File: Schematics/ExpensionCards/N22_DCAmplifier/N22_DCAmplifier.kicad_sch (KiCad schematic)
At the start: 81 parts

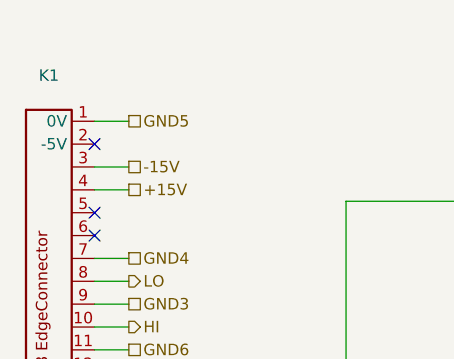
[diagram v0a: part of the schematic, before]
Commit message: Reworked N20/N21
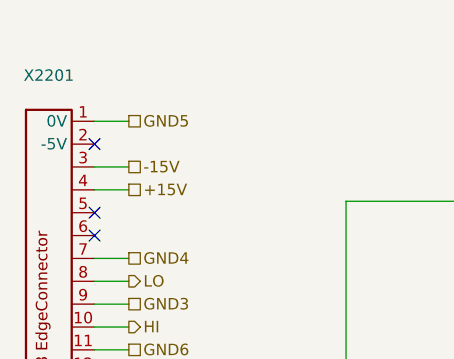
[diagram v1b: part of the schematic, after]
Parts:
- JP2201: renamed from JP2; footprint TestPoint:TestPoint_Bridge_Pitch2.54mm_Drill1.0mm -> TestPoint:TestPoint_Bridge_Pitch5.08mm_Drill0.7mm
- JP2202: renamed from JP1; footprint TestPoint:TestPoint_Bridge_Pitch2.54mm_Drill1.0mm -> TestPoint:TestPoint_Bridge_Pitch5.08mm_Drill0.7mm
- R2209, R2214, R2216, R2217, R2232: footprint PM2528:Potentiometer horizontal ceramic -> PM2528:Trimmer vertical
- renumbered K1 to X2201
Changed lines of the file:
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@@
 		(on_board yes)
 		(dnp no)
-		(property "Reference" "JP2"
+		(property "Reference" "JP2201"
 			(at 90.17 199.39 0)
 			(effects
@@
 			)
 		)
-		(property "Footprint" "TestPoint:TestPoint_Bridge_Pitch2.54mm_Drill1.0mm"
+		(property "Footprint" "TestPoint:TestPoint_Bridge_Pitch5.08mm_Drill0.7mm"
 			(at 90.17 205.74 0)
 			(effects
@@
 			(project "N22_DCAmplifier"
 				(path "/2ba4ca6b-4aec-411c-9da4-218d92fedde9"
-					(reference "JP2")
+					(reference "JP2201")
 					(unit 1)
 				)
@@
 			)
 		)
-		(property "Footprint" "PM2528:Potentiometer horizontal ceramic"
+		(property "Footprint" "PM2528:Trimmer vertical"
 			(at 156.21 193.04 0)
 			(effects
@@
 		(on_board yes)
 		(dnp no)
-		(property "Reference" "JP1"
+		(property "Reference" "JP2202"
 			(at 77.47 199.39 0)
 			(effects
@@
 			)
 		)
-		(property "Footprint" "TestPoint:TestPoint_Bridge_Pitch2.54mm_Drill1.0mm"
+		(property "Footprint" "TestPoint:TestPoint_Bridge_Pitch5.08mm_Drill0.7mm"
 			(at 77.47 205.74 0)
 			(effects
@@
 			(project ""
 				(path "/2ba4ca6b-4aec-411c-9da4-218d92fedde9"
-					(reference "JP1")
+					(reference "JP2202")
 					(unit 1)
 				)
@@
 			)
 		)
-		(property "Footprint" "PM2528:Potentiometer horizontal ceramic"
+		(property "Footprint" "PM2528:Trimmer vertical"
 			(at 110.49 209.55 0)
 			(effects
@@
 			)
 		)
-		(property "Footprint" "PM2528:Potentiometer horizontal ceramic"
+		(property "Footprint" "PM2528:Trimmer vertical"
 			(at 95.25 120.65 0)
 			(effects
@@
 			)
 		)
-		(property "Footprint" "PM2528:Potentiometer horizontal ceramic"
+		(property "Footprint" "PM2528:Trimmer vertical"
 			(at 172.72 88.9 0)
 			(effects
@@
 			)
 		)
-		(property "Footprint" "PM2528:Potentiometer horizontal ceramic"
+		(property "Footprint" "PM2528:Trimmer vertical"
 			(at 76.2 261.62 0)
 			(effects
@@
 		(dnp no)
 		(fields_autoplaced yes)
-		(property "Reference" "K1"
+		(property "Reference" "X2201"
 			(at 20.32 20.32 0)
 			(effects
@@
 					(size 1.27 1.27)
 				)
+				(hide yes)
 			)
 		)
@@
 			(project ""
 				(path "/2ba4ca6b-4aec-411c-9da4-218d92fedde9"
-					(reference "K1")
+					(reference "X2201")
 					(unit 1)
 				)

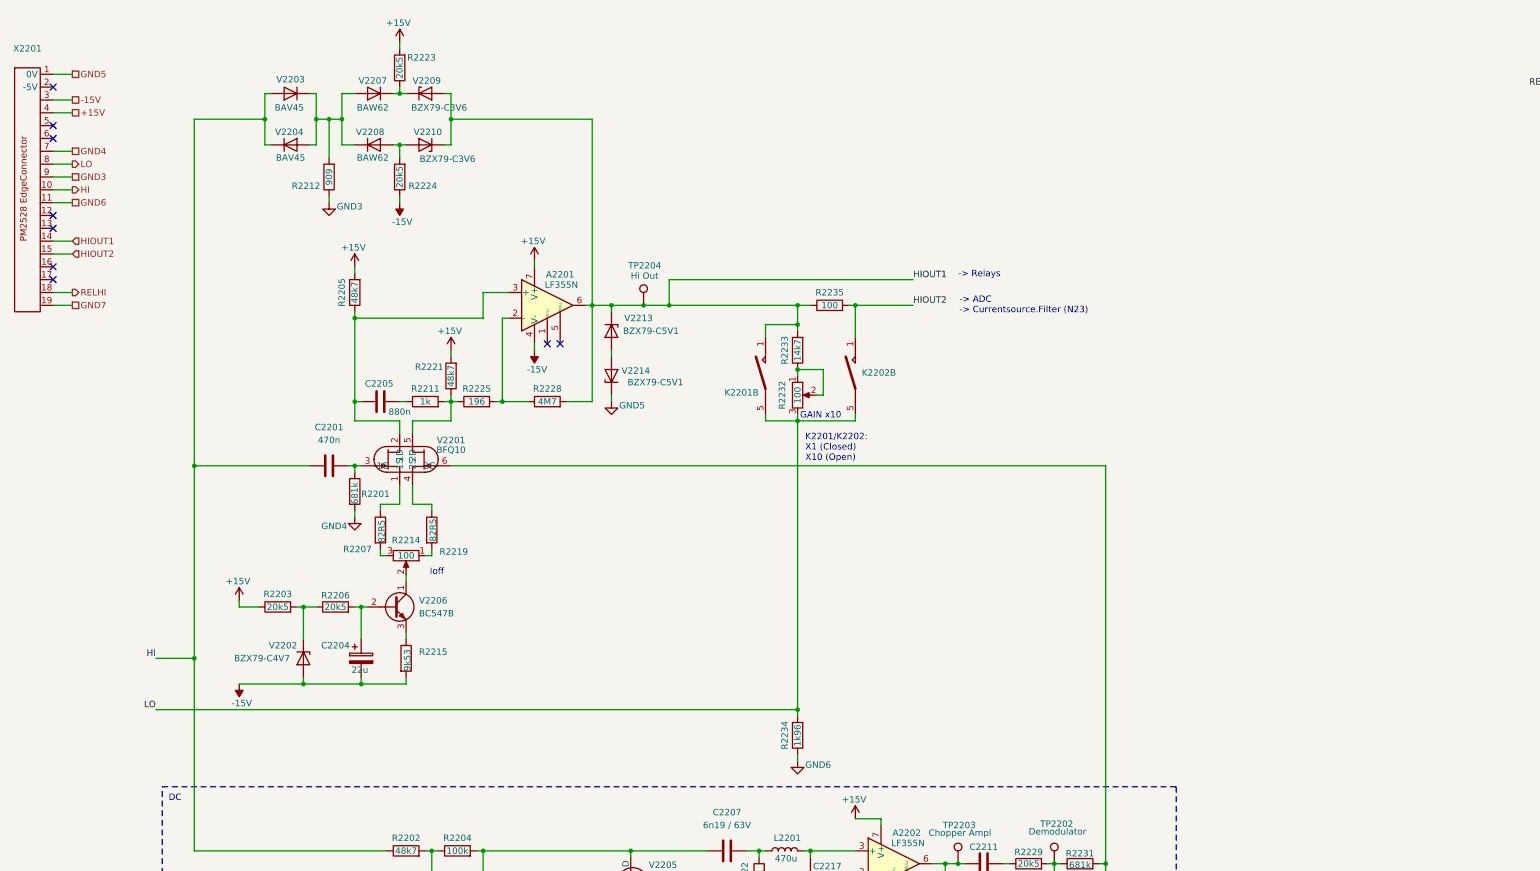
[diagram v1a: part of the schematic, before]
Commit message: Small modifications, more disassembly
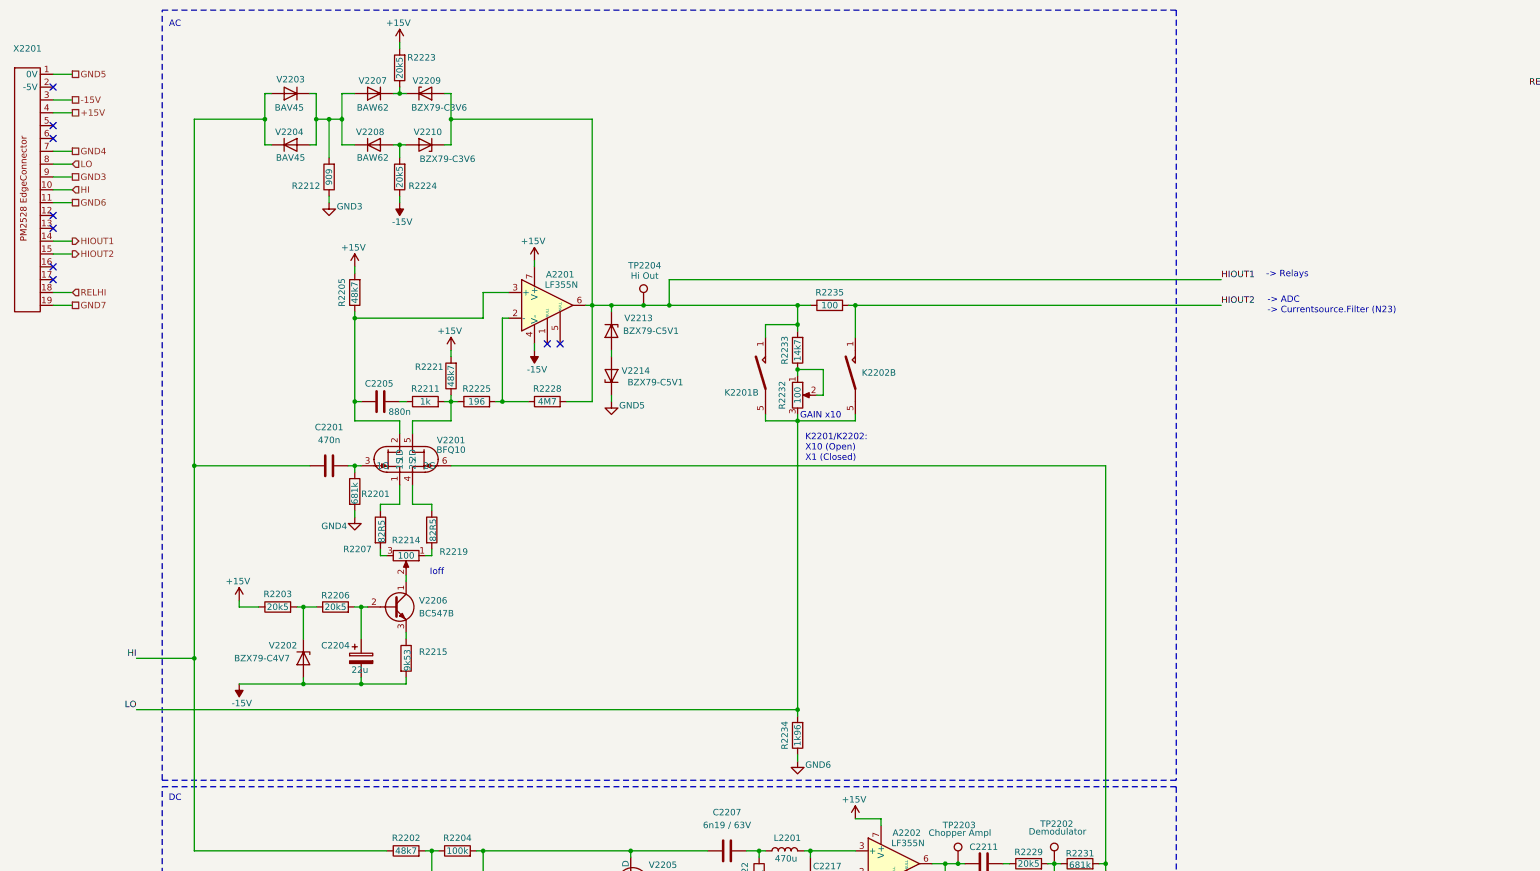
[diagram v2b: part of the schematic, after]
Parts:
- V2203, V2204: footprint Diode_THT:D_DO-35_SOD27_P5.08mm_Vertical_AnodeUp -> Diode_THT:D_DO-35_SOD27_P7.62mm_Horizontal
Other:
- note added: "AC"
- note added: "K2201/K2202: X10 (Open) X1 (Closed)"
- note removed: "K2201/K2202: X1 (Closed) X10 (Open)"
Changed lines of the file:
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@@
 	)
 	(rectangle
+		(start 46.99 12.7)
+		(end 247.65 165.1)
+		(stroke
+			(width 0)
+			(type dash_dot_dot)
+		)
+		(fill
+			(type none)
+		)
+	)
+	(rectangle
 		(start 46.99 218.44)
 		(end 144.78 281.94)
@@
 	(text "-> Relays"
 		(exclude_from_sim no)
-		(at 204.47 65.024 0)
+		(at 265.43 65.024 0)
 		(effects
 			(font
@@
 	(text "-> ADC\n-> Currentsource.Filter (N23)\n"
 		(exclude_from_sim no)
-		(at 204.724 71.12 0)
+		(at 265.684 71.12 0)
 		(effects
 			(font
@@
 		)
 	)
-	(text "K2201/K2202:\nX1 (Closed)\nX10 (Open)"
+	(text "K2201/K2202:\nX10 (Open)\nX1 (Closed)\n"
 		(exclude_from_sim no)
 		(at 174.244 99.314 0)
@@
 		)
 	)
+	(text "AC"
+		(exclude_from_sim no)
+		(at 49.53 15.494 0)
+		(effects
+			(font
+				(size 1.27 1.27)
+			)
+		)
+	)
 	(text "Power"
 		(exclude_from_sim no)
@@
 	(wire
 		(pts
-			(xy 195.58 66.04) (xy 147.32 66.04)
+			(xy 256.54 66.04) (xy 147.32 66.04)
 		)
 		(stroke
@@
 	(wire
 		(pts
-			(xy 184.15 71.12) (xy 195.58 71.12)
+			(xy 184.15 71.12) (xy 256.54 71.12)
 		)
 		(stroke
@@
 	(wire
 		(pts
-			(xy 45.72 140.97) (xy 53.34 140.97)
+			(xy 41.91 140.97) (xy 53.34 140.97)
 		)
 		(stroke
@@
 	(wire
 		(pts
-			(xy 45.72 151.13) (xy 172.72 151.13)
+			(xy 41.91 151.13) (xy 172.72 151.13)
 		)
 		(stroke
@@
 	)
 	(label "HI"
-		(at 45.72 140.97 180)
+		(at 41.91 140.97 180)
 		(effects
 			(font
@@
 	)
 	(label "HIOUT1"
-		(at 195.58 66.04 0)
+		(at 256.54 66.04 0)
 		(effects
 			(font
@@
 	)
 	(label "LO"
-		(at 45.72 151.13 180)
+		(at 41.91 151.13 180)
 		(effects
 			(font
@@
 	)
 	(label "HIOUT2"
-		(at 195.58 71.12 0)
+		(at 256.54 71.12 0)
 		(effects
 			(font
@@
 	)
 	(hierarchical_label "HIOUT2"
-		(shape input)
+		(shape output)
 		(at 29.21 60.96 0)
 		(effects
@@
 	)
 	(hierarchical_label "HI"
-		(shape output)
+		(shape input)
 		(at 29.21 48.26 0)
 		(effects
@@
 	)
 	(hierarchical_label "RELHI"
-		(shape output)
+		(shape input)
 		(at 29.21 68.58 0)
 		(effects
@@
 	)
 	(hierarchical_label "LO"
-		(shape output)
+		(shape input)
 		(at 29.21 43.18 0)
 		(effects
@@
 	)
 	(hierarchical_label "HIOUT1"
-		(shape input)
+		(shape output)
 		(at 29.21 58.42 0)
 		(effects
@@
 			)
 		)
-		(property "Footprint" "Diode_THT:D_DO-35_SOD27_P5.08mm_Vertical_AnodeUp"
+		(property "Footprint" "Diode_THT:D_DO-35_SOD27_P7.62mm_Horizontal"
 			(at 72.39 24.765 0)
 			(effects
@@
 				)
 				(justify left)
+				(hide yes)
 			)
 		)
@@
 			)
 		)
-		(property "Footprint" "Diode_THT:D_DO-35_SOD27_P5.08mm_Vertical_AnodeUp"
+		(property "Footprint" "Diode_THT:D_DO-35_SOD27_P7.62mm_Horizontal"
 			(at 72.39 43.815 0)
 			(effects
@@
 				)
 				(justify left)
+				(hide yes)
 			)
 		)
